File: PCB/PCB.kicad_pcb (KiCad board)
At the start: 2 copper layers, 120 x 60 mm, 62 parts, among them J1 USB_C_Receptacle_USB2.0_16P, J2 Conn_01x15, J3 Conn_01x15, Q2 IRLML2060, SW1 TSA016A2526B, SW2 TSA016A2526B, SW3 TSA016A2526B, U1 RP2040, U2 USBLC6-2SC6, U3 NCP1117ST33T3G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

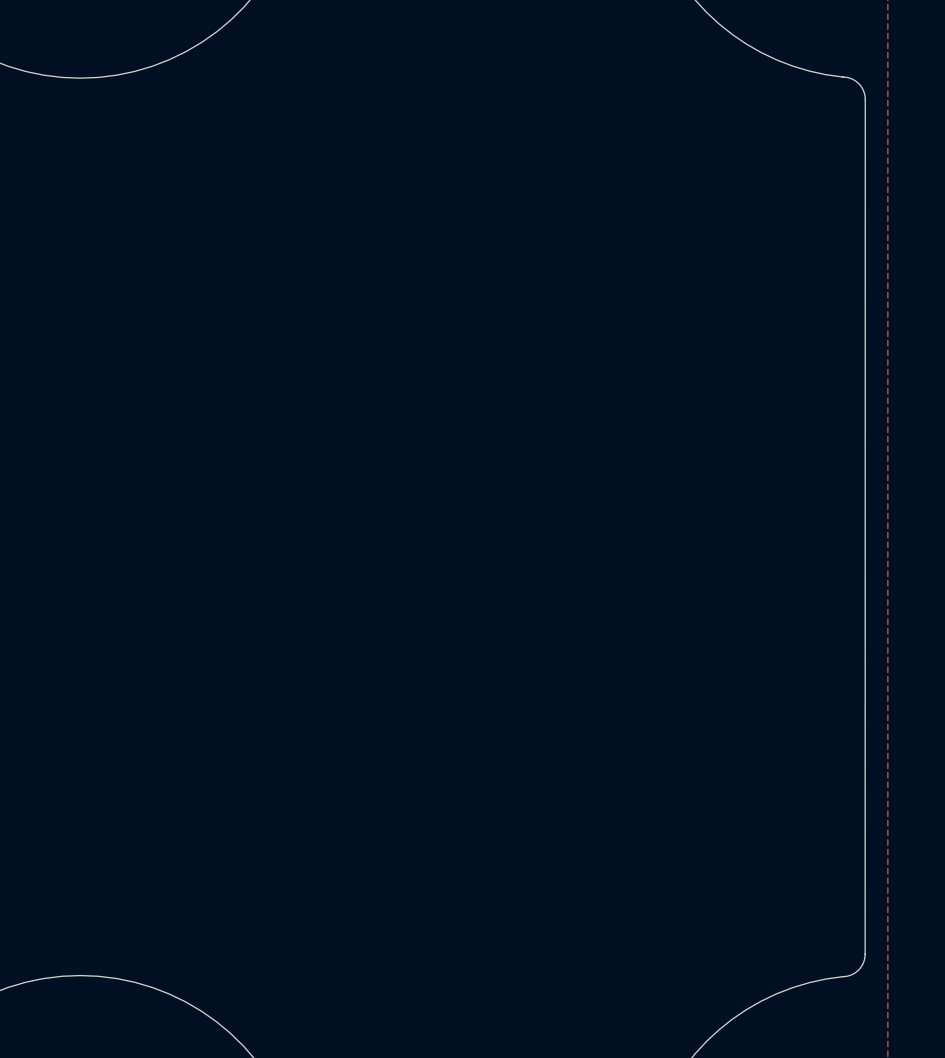
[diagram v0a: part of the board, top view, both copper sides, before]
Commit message: added the NFC antenna in
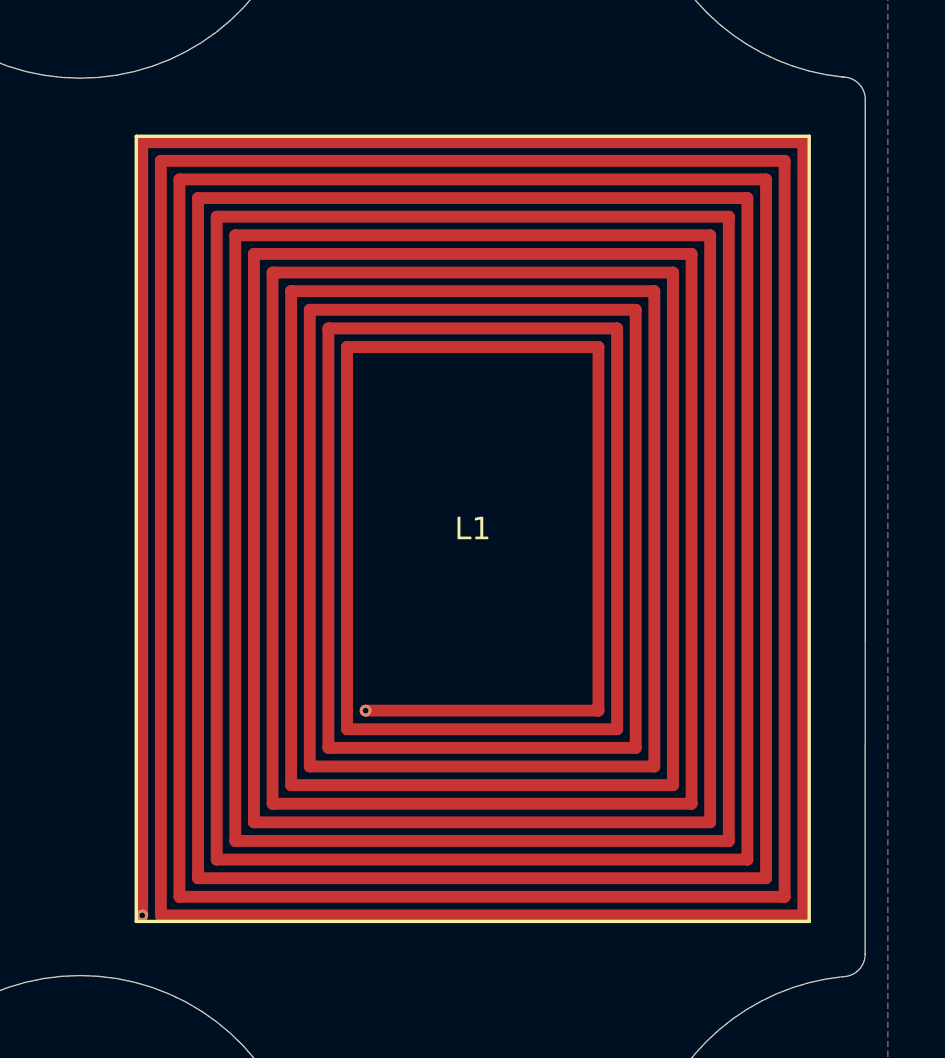
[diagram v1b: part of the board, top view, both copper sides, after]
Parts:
- added L1: NFC Antenna, nfc:30x35mm-antenna, F.Cu at (157.5, 107.6)

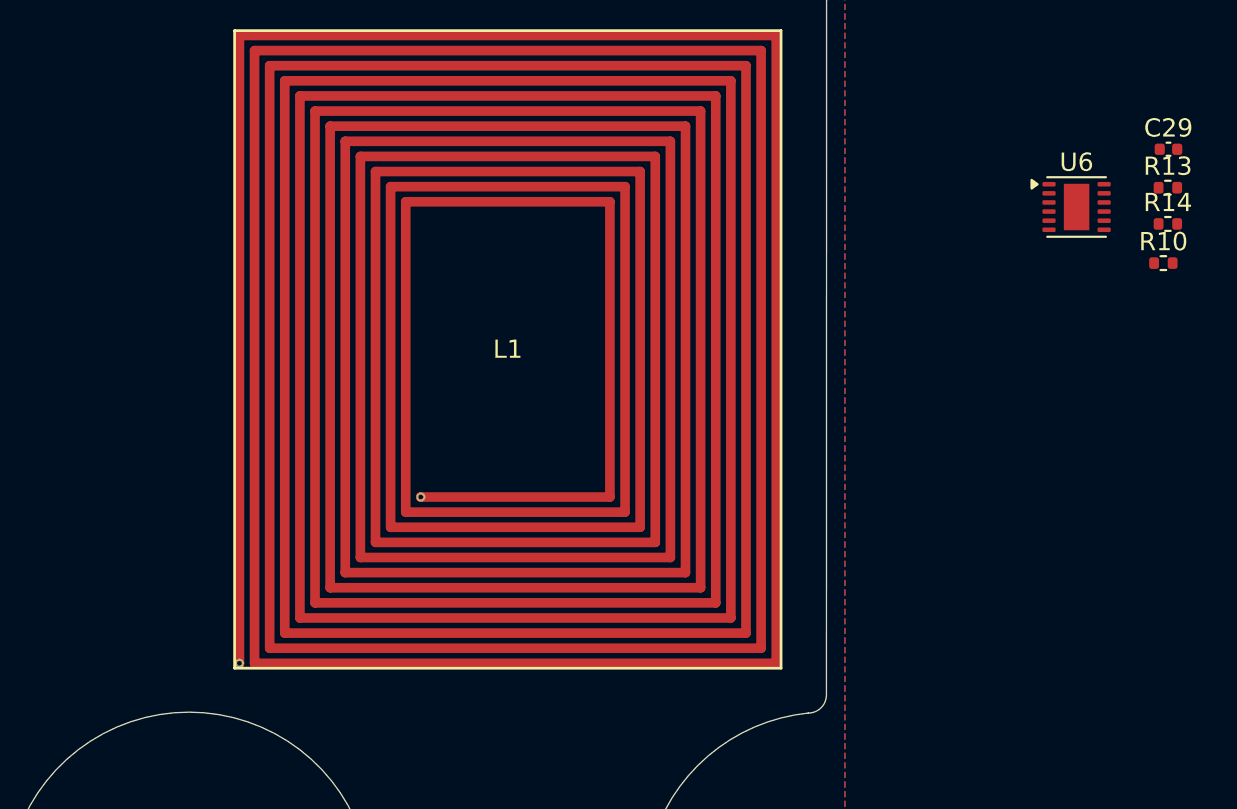
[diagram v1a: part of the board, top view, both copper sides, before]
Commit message: placed the NFC IC and routed it
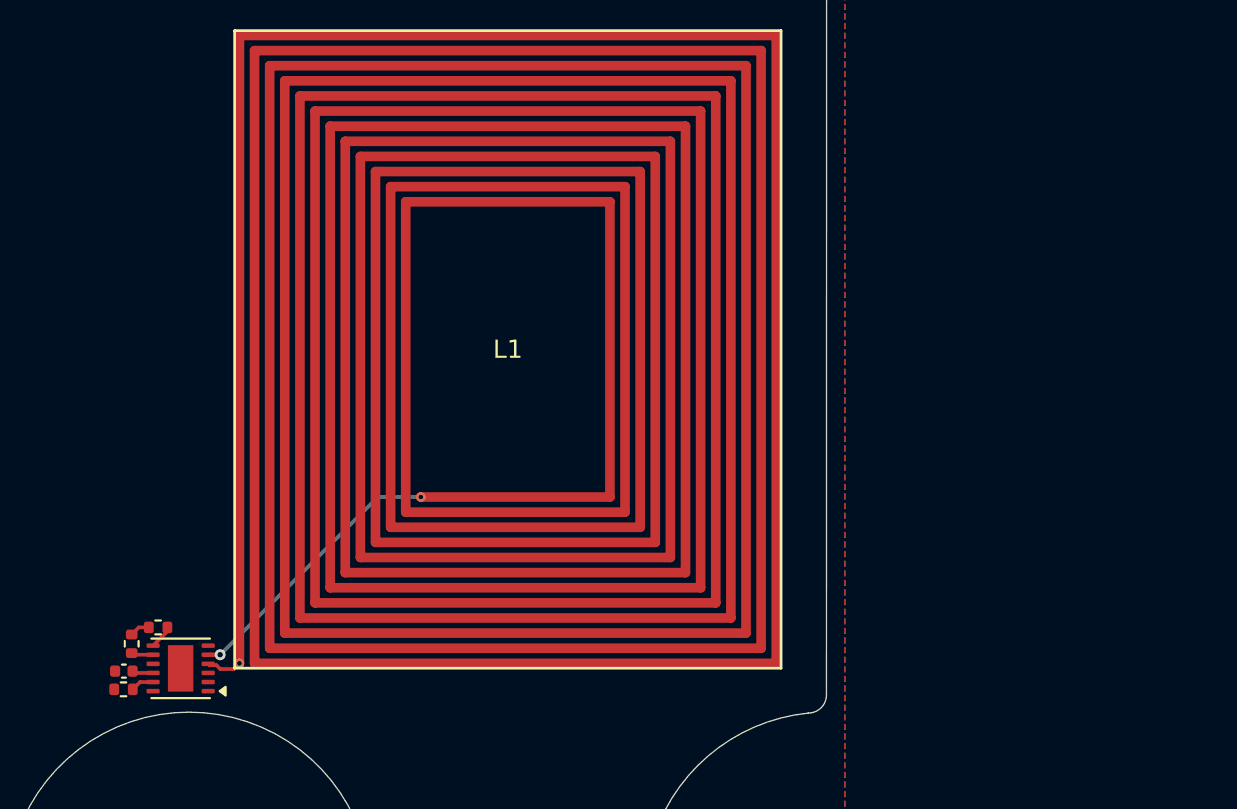
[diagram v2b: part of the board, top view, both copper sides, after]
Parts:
- moved C29 64.1 mm to (151.4, 142.8)
- moved R14 62.8 mm to (151.4, 143.8)
- moved R13 62.2 mm to (151.8, 141.2), turned to -90 degrees
- moved R10 58.7 mm to (153.3, 140.3)
- moved U6 55.3 mm to (154.5, 142.6), turned to 180 degrees
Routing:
- net Net-(U6-AC1): track 0.00 -> 15.3 mm, vias 0 -> 1
- net +3V3: track 0.00 -> 2.27 mm
- net Net-(U6-AC0): track 0.00 -> 1.96 mm
- net /NFC_SDA: track 0.00 -> 1.33 mm
- net /NFC_GPO: track 0.00 -> 1.28 mm
- net /NFC_SCL: track 0.00 -> 1.21 mm

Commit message: working on a new shape
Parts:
- moved R10 1.61 mm to (152.3, 139.1)
- moved R13 1.30 mm to (152.3, 140.1), turned to 0 degrees
- moved R14 0.27 mm to (151.2, 143.6)
- moved C29 0.27 mm to (151.2, 142.6)
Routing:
- net Net-(U6-AC1): track 15.3 -> 0.00 mm, vias 1 -> 0
- net +3V3: track 2.27 -> 0.00 mm
- net Net-(U6-AC0): track 1.96 -> 0.00 mm
- net /NFC_SDA: track 1.33 -> 0.00 mm
- net /NFC_GPO: track 1.28 -> 0.00 mm
- net /NFC_SCL: track 1.21 -> 0.00 mm
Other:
- board size 120 x 60 mm -> 166.1 x 129.3 mm

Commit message: more decorational shapes
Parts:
- moved J2 75.4 mm to (123.0, 83.3)
- moved J3 75.4 mm to (158.6, 26.9)
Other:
- board size 166.1 x 129.3 mm -> 148.3 x 129.9 mm

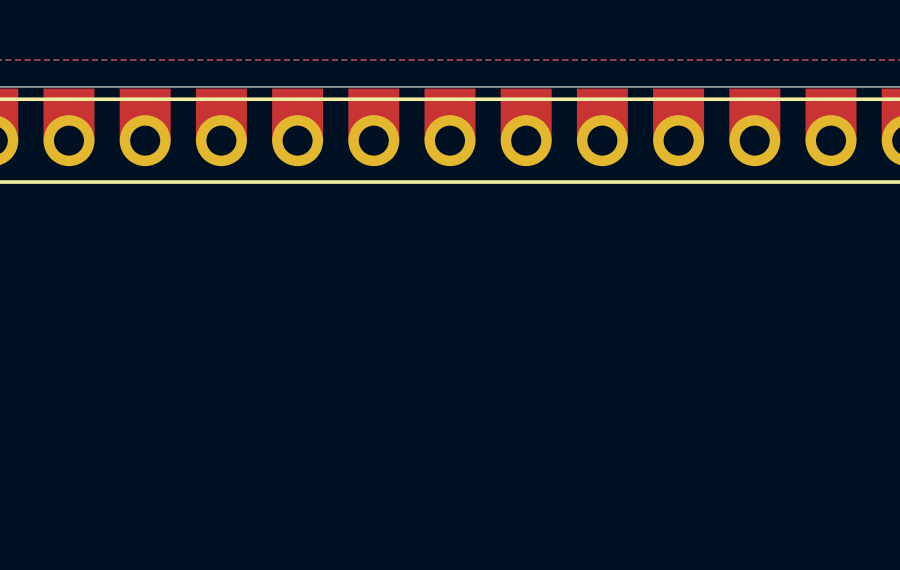
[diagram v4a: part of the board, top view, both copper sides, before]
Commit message: doing this cool effect on the fill, have to make it work with GND instead though
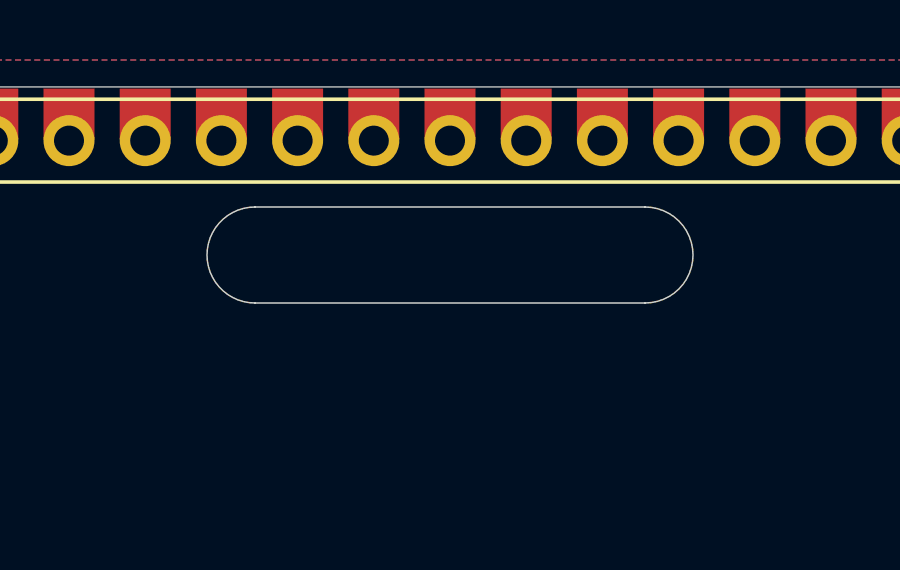
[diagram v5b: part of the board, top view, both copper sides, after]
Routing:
- added copper zone on B.Cu, net (none)
- added copper zone on F.Cu, net (none)
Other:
- outline, holes or cut-outs redrawn
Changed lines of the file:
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@@
+		(layer "Edge.Cuts")
+	)
+	(gr_arc
+		(start 147.317629 29.1)
+		(mid 148.9176 30.7)
+		(end 147.317629 32.3)
+		(stroke
+			(width 0.05)
+			(type default)
+		)
 		(layer "Edge.Cuts")
 	)
@@
 		(layer "Edge.Cuts")
 	)
+	(gr_line
+		(start 134.317629 32.3)
+		(end 147.317629 32.3)
+		(stroke
+			(width 0.05)
+			(type default)
+		)
+		(layer "Edge.Cuts")
+	)
 	(gr_arc
 		(start 174.08114 25.097818)
@@
 		(stroke
 			(width 0.01)
+			(type default)
+		)
+		(layer "Edge.Cuts")
+	)
+	(gr_arc
+		(start 134.317629 32.3)
+		(mid 132.7176 30.7)
+		(end 134.317629 29.1)
+		(stroke
+			(width 0.05)
+			(type default)
+		)
+		(layer "Edge.Cuts")
+	)
+	(gr_line
+		(start 147.317629 29.1)
+		(end 134.317629 29.1)
+		(stroke
+			(width 0.05)
 			(type default)
 		)
@@
 	)
 	(zone
-		(net 2)
-		(net_name "GND")
+		(net 0)
+		(net_name "")
 		(layers "F.Cu" "B.Cu")
 		(hatch edge 0.5)
@@
 			(thermal_gap 0.5)
 			(thermal_bridge_width 0.5)
+			(island_removal_mode 1)
+			(island_area_min 10)
 		)
 		(polygon
@@
 		)
 	)
+	(group ""
+		(members "162ab123-923f-4e19-be61-0324decd1f67" "1efb17f0-22fb-40ea-8807-f4fe69c3b792"
+			"b7a0f540-713e-4c9b-964d-49741287ba49" "b864c2af-c021-4858-a3a0-57c0e8108585"
+		)
+	)

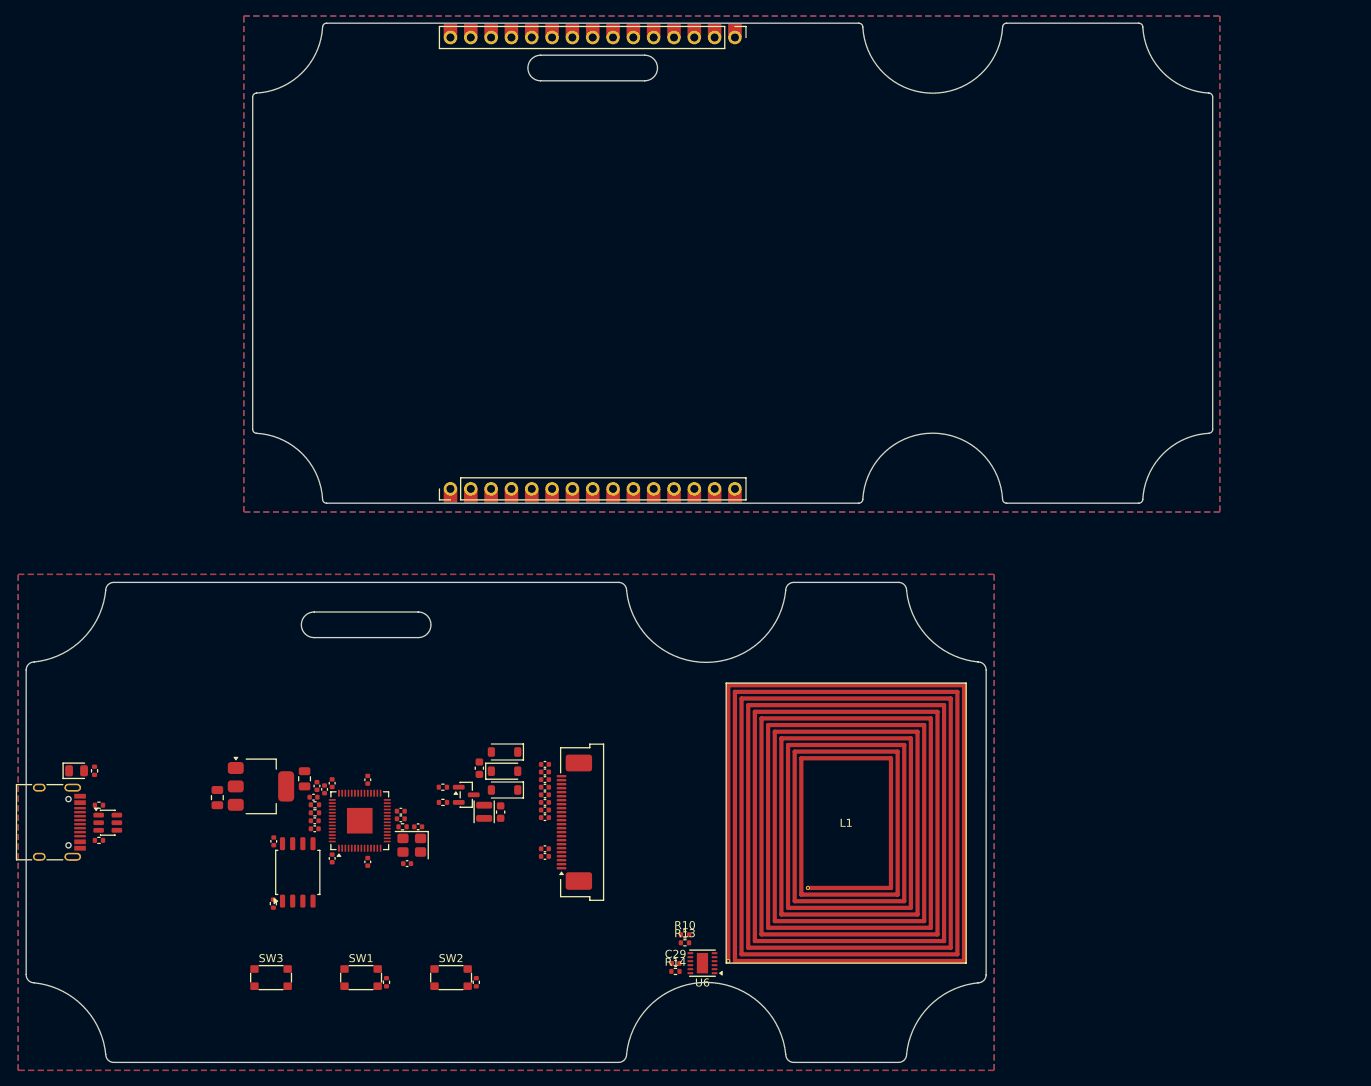
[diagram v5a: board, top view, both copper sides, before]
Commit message: re-organizing most of the components
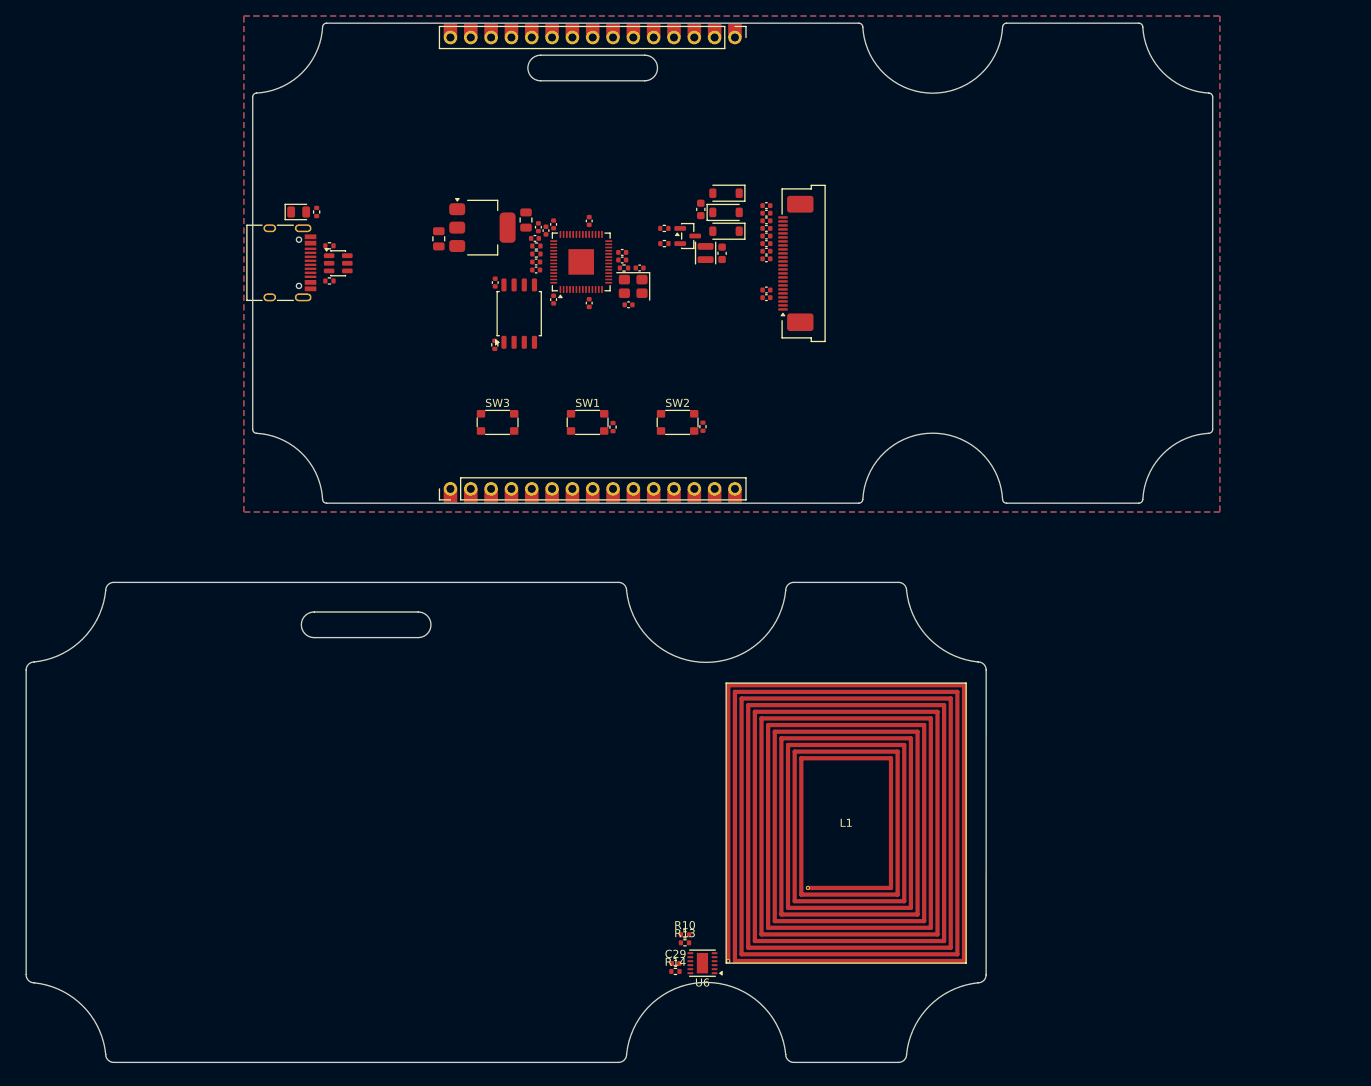
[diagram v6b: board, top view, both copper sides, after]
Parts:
- moved J1 75.6 mm to (101.5, 55.0)
- moved R2 75.6 mm to (107.9, 57.3)
- moved R1 75.6 mm to (107.9, 52.9)
- moved U2 75.6 mm to (109.0, 55.1)
- moved D1 75.2 mm to (104.1, 48.7)
- moved R7 75.2 mm to (106.3, 48.7)
- moved C10 75.1 mm to (135.0, 51.0)
- moved C1 75.1 mm to (121.6, 52.1)
- moved C13 75.1 mm to (133.8, 56.0)
- moved C14 75.1 mm to (145.3, 60.3)
- moved C15 75.1 mm to (146.7, 55.7)
- moved C16 75.1 mm to (128.6, 57.5)
- moved C17 75.1 mm to (162.5, 59.4)
- moved C18 75.1 mm to (162.5, 58.5)
- moved C19 75.1 mm to (162.5, 54.6)
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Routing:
- removed copper zone on B.Cu, net (none)
- removed copper zone on F.Cu, net (none)
